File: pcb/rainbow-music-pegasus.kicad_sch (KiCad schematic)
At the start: 32 parts, among them J1 USB_B_Micro, J2 Conn_02x03_Odd_Even, U1 ESP32-C3-MINI-1, U2 OPA340NA, U3 AP2204RB-3.3

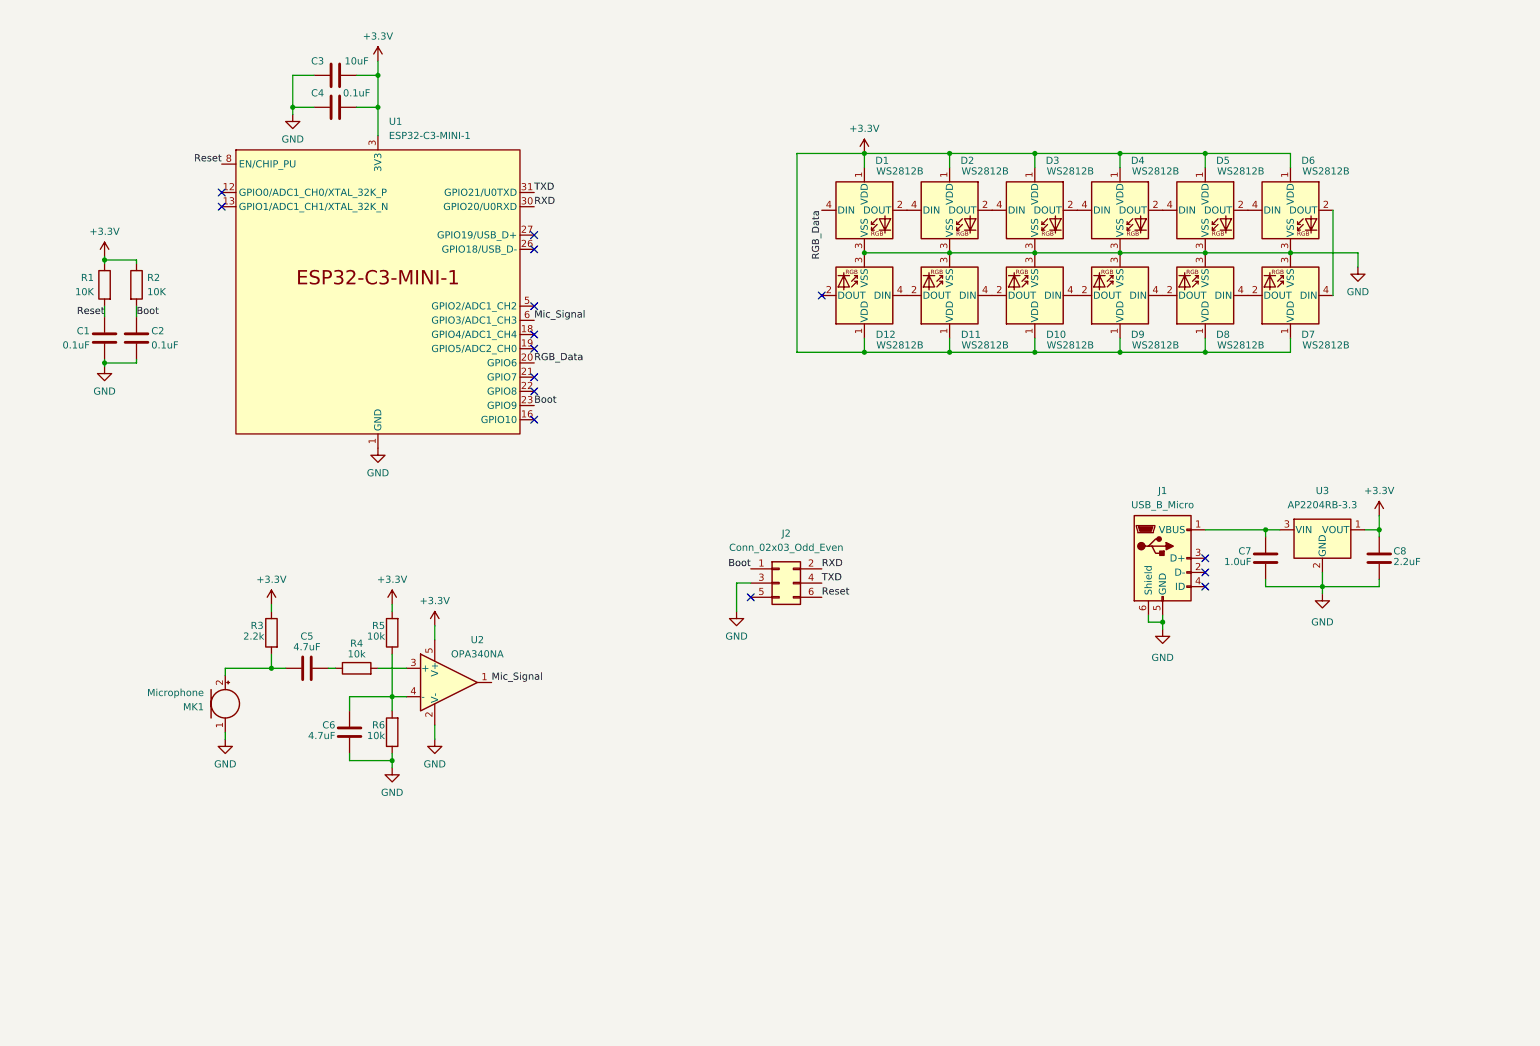
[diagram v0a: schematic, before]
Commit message: Working PCB design using esp32c3 and 20 ws2812b LEDs -- BOM pending validation
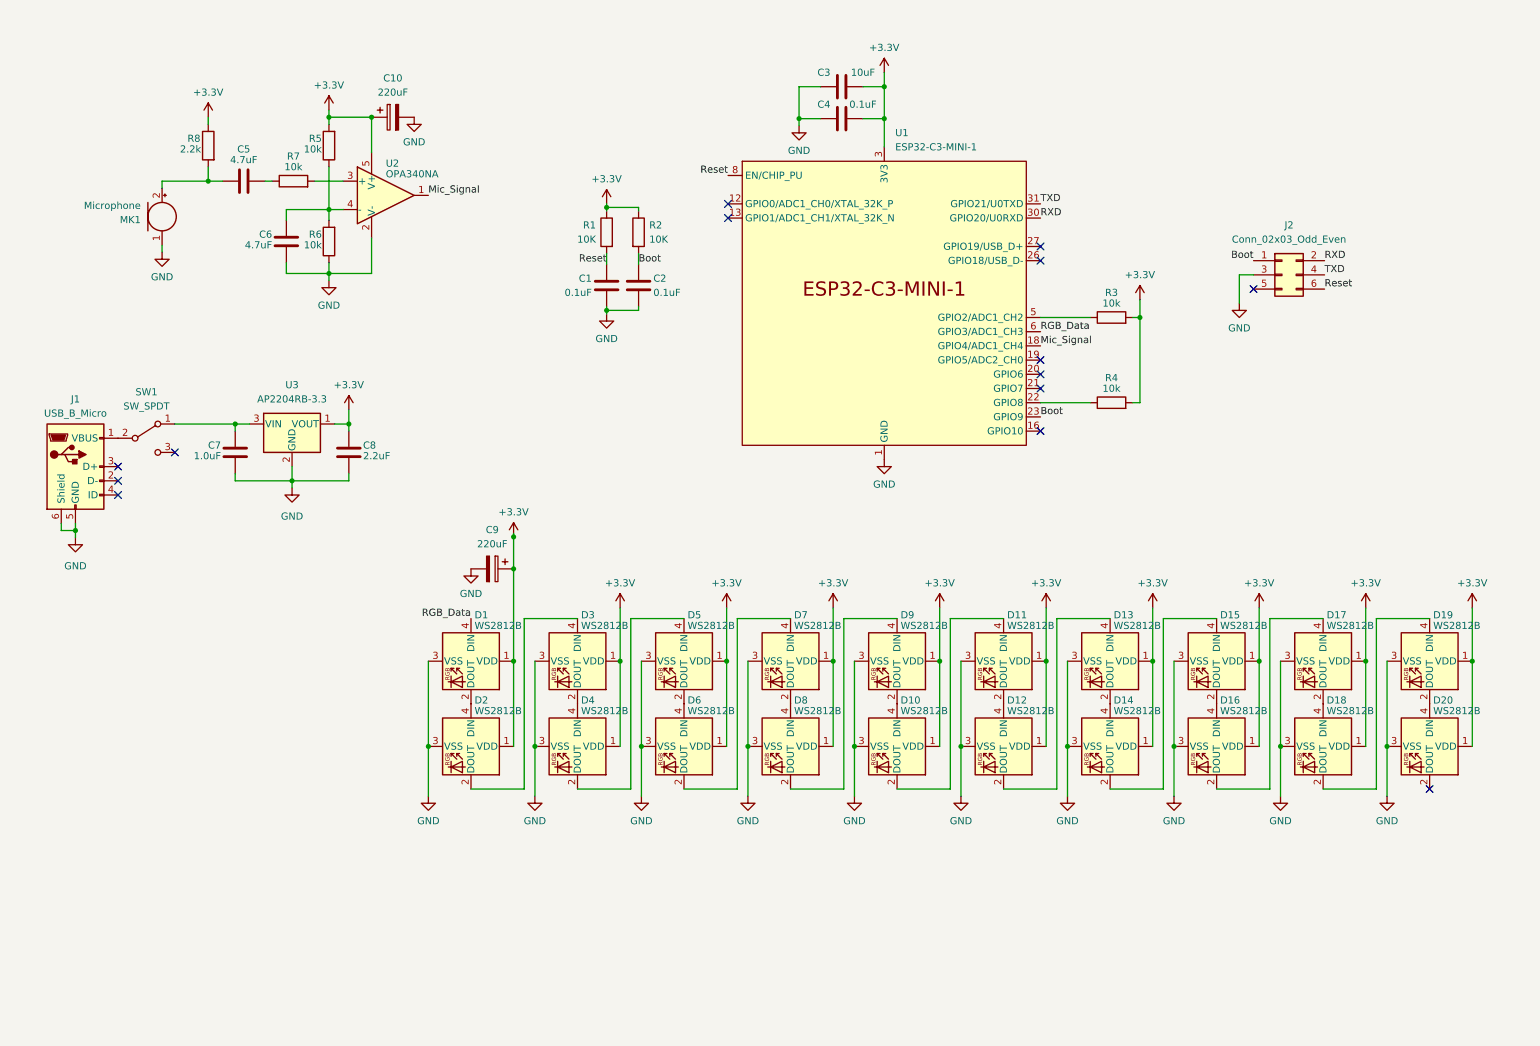
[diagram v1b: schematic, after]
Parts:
- removed D2: WS2812B, LED_SMD:LED_WS2812B_PLCC4_5.0x5.0mm_P3.2mm, symbol LED:WS2812B
- added C10, C9: 220uF, Capacitor_SMD:CP_Elec_4x3, symbol Device:C_Polarized
- added D12, D13, D14, D15, D16, D17, D18, D19, D20: WS2812B, LED_SMD:LED_WS2812B_PLCC4_5.0x5.0mm_P3.2mm, symbol LED:WS2812B
- added R3, R4: 10k, Resistor_SMD:R_0805_2012Metric, symbol Device:R
- added SW1: SW_SPDT, Button_Switch_THT:SW_CuK_OS102011MA1QN1_SPDT_Angled, symbol Switch:SW_SPDT
- renumbered D12 to D2, R4 to R7, R3 to R8
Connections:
- net +3.3V: now also C10.1, C9.1, D12.1 (VDD), D13.1 (VDD), D14.1 (VDD), D15.1 (VDD), D16.1 (VDD), D17.1 (VDD), D18.1 (VDD), D19.1 (VDD), D20.1 (VDD), R3.2, R4.2
- net GND: now also C10.2, C9.2, D12.3 (VSS), D13.3 (VSS), D14.3 (VSS), D15.3 (VSS), D16.3 (VSS), D17.3 (VSS), D18.3 (VSS), D19.3 (VSS), D20.3 (VSS)
- net Mic_Signal: now also U1.18 (GPIO4/ADC1_CH4); no longer U1.6 (GPIO3/ADC1_CH3)
- net RGB_Data: now also U1.6 (GPIO3/ADC1_CH3); no longer U1.20 (GPIO6)
- net at D3.4 (DIN): now also D2.2 (DOUT)
- net at D2.4 (DIN): now also D1.2 (DOUT); no longer D11.2 (DOUT)
- net at U1.22 (GPIO8): now also R4.1
- net at U1.5 (GPIO2/ADC1_CH2): now also R3.1
- net at C7.2, U3.3 (VIN): now also SW1.1 (A); no longer J1.1 (VBUS)
- new net: D15.2 (DOUT), D16.4 (DIN)
- new net: D14.2 (DOUT), D15.4 (DIN)
- new net: D17.2 (DOUT), D18.4 (DIN)
- new net: D16.2 (DOUT), D17.4 (DIN)
- new net: D19.2 (DOUT), D20.4 (DIN)
- new net: J1.1 (VBUS), SW1.2 (B)
- new net: D11.2 (DOUT), D12.4 (DIN)
- new net: D18.2 (DOUT), D19.4 (DIN)
- new net: D12.2 (DOUT), D13.4 (DIN)
- new net: D13.2 (DOUT), D14.4 (DIN)
- no-connect marks 15 -> 14
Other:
- moved on the sheet: C1, C2, C3, C4, C5, C6, C7, C8, D1, D2, J1, J2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

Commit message: Finalize PCB layout for first production run
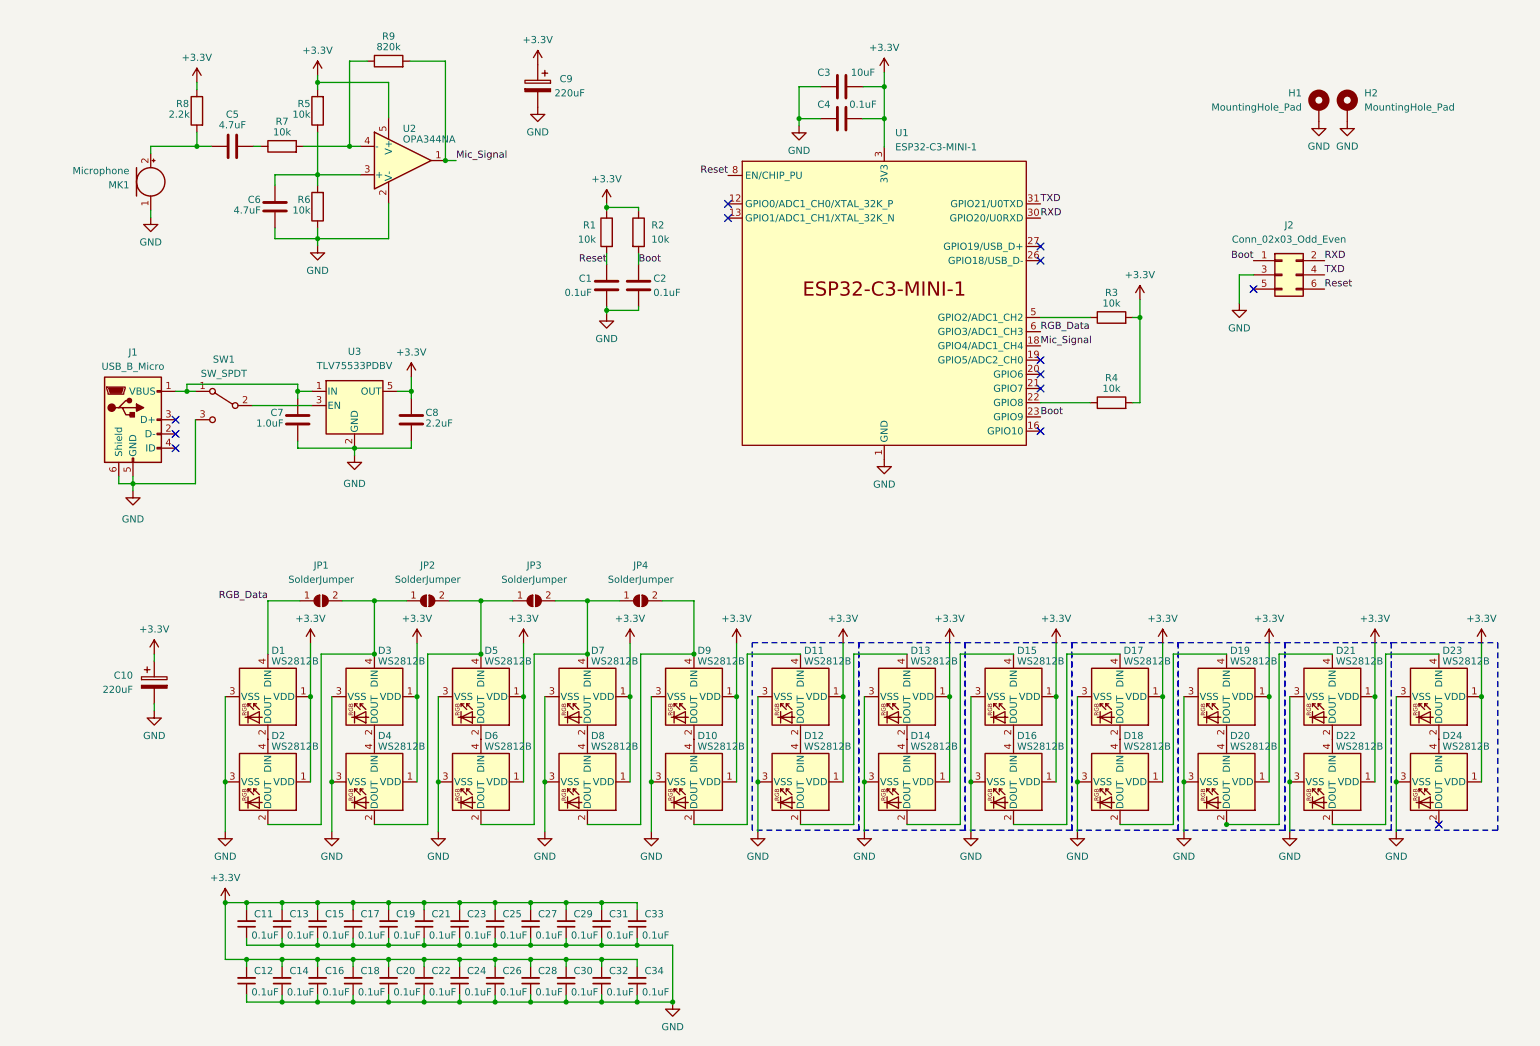
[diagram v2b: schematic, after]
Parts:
- removed U3: AP2204RB-3.3, Package_TO_SOT_SMD:SOT-89-3, symbol Regulator_Linear:AP2204RB-3.3
- added C11, C12, C13, C14, C15, C16, C17, C18, C19, C20, C21, C22, C23, C24, C25, C26, C27, C28, C29, C30, C31, C32, C33, C34: 0.1uF, Capacitor_SMD:C_0603_1608Metric, symbol Device:C_Small
- added D21, D22, D23, D24: WS2812B, LED_SMD:LED_WS2812B_PLCC4_5.0x5.0mm_P3.2mm, symbol LED:WS2812B
- added H1, H2: MountingHole_Pad, MountingHole:MountingHole_2.2mm_M2_Pad_Via, symbol Mechanical:MountingHole_Pad
- added JP1, JP2, JP3, JP4: SolderJumper, Jumper:SolderJumper-2_P1.3mm_Open_TrianglePad1.0x1.5mm, symbol Jumper:SolderJumper_2_Open
- added R9: 820k, Resistor_SMD:R_0805_2012Metric, symbol Device:R
- added U3: TLV75533PDBV, Package_TO_SOT_SMD:SOT-23-5, symbol Regulator_Linear:TLV75533PDBV
- C10: renamed from C9; footprint Capacitor_SMD:CP_Elec_4x3 -> Capacitor_SMD:CP_Elec_5x5.9
- C9: renamed from C10; footprint Capacitor_SMD:CP_Elec_4x3 -> Capacitor_SMD:CP_Elec_5x5.9
- R1, R2: value 10K -> 10k
- U2: value OPA340NA -> OPA344NA
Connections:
- net +3.3V: now also C11.2, C12.2, C13.2, C14.2, C15.2, C16.2, C17.2, C18.2, C19.2, C20.2, C21.2, C22.2, C23.2, C24.2, C25.2, C26.2, C27.2, C28.2, C29.2, C30.2, C31.2, C32.2, C33.2, C34.2, D21.1 (VDD), D22.1 (VDD), D23.1 (VDD), D24.1 (VDD), U3.5 (OUT)
- net GND: now also SW1.3 (C), C11.1, C12.1, C13.1, C14.1, C15.1, C16.1, C17.1, C18.1, C19.1, C20.1, C21.1, C22.1, C23.1, C24.1, C25.1, C26.1, C27.1, C28.1, C29.1, C30.1, C31.1, C32.1, C33.1, C34.1, D21.3 (VSS), D22.3 (VSS), D23.3 (VSS), D24.3 (VSS), H1.1, H2.1, U3.2 (GND)
- net Mic_Signal: now also R9.2
- net RGB_Data: now also JP1.1 (A)
- net at D2.2 (DOUT), D3.4 (DIN): now also JP1.2 (B), JP2.1 (A)
- net at D8.2 (DOUT), D9.4 (DIN): now also JP4.2 (B)
- net at R7.2: now also U2.4 (-), R9.1; no longer U2.3 (+)
- net at C6.2, R5.1, R6.2: now also U2.3 (+); no longer U2.4 (-)
- net at D6.2 (DOUT), D7.4 (DIN): now also JP3.2 (B), JP4.1 (A)
- net at D20.2 (DOUT): now also D21.4 (DIN)
- net at J1.1 (VBUS): now also C7.2, SW1.1 (A), U3.1 (IN); no longer SW1.2 (B)
- net at D4.2 (DOUT), D5.4 (DIN): now also JP2.2 (B), JP3.1 (A)
- new net: SW1.2 (B), U3.3 (EN)
- new net: D23.2 (DOUT), D24.4 (DIN)
- new net: D22.2 (DOUT), D23.4 (DIN)
- new net: D21.2 (DOUT), D22.4 (DIN)
- no-connect marks 14 -> 13
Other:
- moved on the sheet: C10, C5, C6, C7, C8, C9, D1, D10, D11, D12, D13, D14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

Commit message: Added a few test points for power.  Committing gerbers
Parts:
- added TP1, TP2, TP3: TestPoint, TestPoint:TestPoint_THTPad_1.5x1.5mm_Drill0.7mm, symbol Connector:TestPoint
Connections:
- net +3.3V: now also TP2.1
- net GND: now also TP3.1
- net at C7.2, J1.1 (VBUS), SW1.1 (A)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: now also TP1.1
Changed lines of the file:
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@@
   (junction (at 62.23 182.88) (diameter 0) (color 0 0 0 0)
   )
+  (junction (at 65.024 80.01) (diameter 0) (color 0 0 0 0)
+  )
   (junction (at 257.683 135.89) (diameter 0) (color 0 0 0 0)
   )
@@
   )
   (junction (at 105.41 135.89) (diameter 0) (color 0 0 0 0)
+  )
+  (junction (at 85.344 91.44) (diameter 0) (color 0 0 0 0)
   )
   (junction (at 87.63 180.34) (diameter 0) (color 0 0 0 0)
@@
     (stroke (width 0) (type default))
   )
+  (wire (pts (xy 65.024 76.2) (xy 65.024 80.01))
+    (stroke (width 0) (type default))
+  )
   (wire (pts (xy 154.686 32.512) (xy 154.686 26.797))
     (stroke (width 0) (type default))
@@
         (path "/4cbaa20b-39f5-487e-a5d4-6b04539cf52b"
           (reference "C19") (unit 1)
+        )
+      )
+    )
+  )
+  (symbol (lib_id "Connector:TestPoint") (at 85.344 91.44 0) (mirror x) (unit 1)
+    (in_bom yes) (on_board yes) (dnp no)
+    (property "Reference" "TP3" (at 86.614 96.012 0)
+      (effects (font (size 1.27 1.27)) (justify left))
+    )
+    (property "Value" "TestPoint" (at 86.614 93.472 0)
+      (effects (font (size 1.27 1.27)) (justify left))
+    )
+    (property "Footprint" "TestPoint:TestPoint_THTPad_1.5x1.5mm_Drill0.7mm" (at 90.424 91.44 0)
+      (effects (font (size 1.27 1.27)) hide)
+    )
+    (property "Datasheet" "~" (at 90.424 91.44 0)
+      (effects (font (size 1.27 1.27)) hide)
+    )
+    (pin "1")
+    (instances
+      (project "rainbow-music-pegasus"
+        (path "/4cbaa20b-39f5-487e-a5d4-6b04539cf52b"
+          (reference "TP3") (unit 1)
         )
       )
@@
     )
   )
+  (symbol (lib_id "Connector:TestPoint") (at 65.024 76.2 0) (mirror y) (unit 1)
+    (in_bom yes) (on_board yes) (dnp no)
+    (property "Reference" "TP1" (at 63.754 71.628 0)
+      (effects (font (size 1.27 1.27)) (justify left))
+    )
+    (property "Value" "TestPoint" (at 63.754 74.168 0)
+      (effects (font (size 1.27 1.27)) (justify left))
+    )
+    (property "Footprint" "TestPoint:TestPoint_THTPad_1.5x1.5mm_Drill0.7mm" (at 59.944 76.2 0)
+      (effects (font (size 1.27 1.27)) hide)
+    )
+    (property "Datasheet" "~" (at 59.944 76.2 0)
+      (effects (font (size 1.27 1.27)) hide)
+    )
+    (pin "1")
+    (instances
+      (project "rainbow-music-pegasus"
+        (path "/4cbaa20b-39f5-487e-a5d4-6b04539cf52b"
+          (reference "TP1") (unit 1)
+        )
+      )
+    )
+  )
   (symbol (lib_id "power:GND") (at 68.58 55.245 0) (unit 1)
     (in_bom yes) (on_board yes) (dnp no) (fields_autoplaced)
@@
         )
       )
+    )
+  )
+  (symbol (lib_id "Connector:TestPoint") (at 85.344 81.28 270) (mirror x) (unit 1)
+    (in_bom yes) (on_board yes) (dnp no)
+    (property "Reference" "TP2" (at 89.916 80.518 90)
+      (effects (font (size 1.27 1.27)) (justify left))
+    )
+    (property "Value" "TestPoint" (at 89.916 82.55 90)
+      (effects (font (size 1.27 1.27)) (justify left))
+    )
+    (property "Footprint" "TestPoint:TestPoint_THTPad_1.5x1.5mm_Drill0.7mm" (at 85.344 76.2 0)
+      (effects (font (size 1.27 1.27)) hide)
+    )
+    (property "Datasheet" "~" (at 85.344 76.2 0)
+      (effects (font (size 1.27 1.27)) hide)
+    )
+    (pin "1")
+    (instances
+      (project "rainbow-music-pegasus"
+        (path "/4cbaa20b-39f5-487e-a5d4-6b04539cf52b"
+          (reference "TP2") (unit 1)
+        )
+      )
